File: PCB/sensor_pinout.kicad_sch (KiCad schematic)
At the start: 0 parts

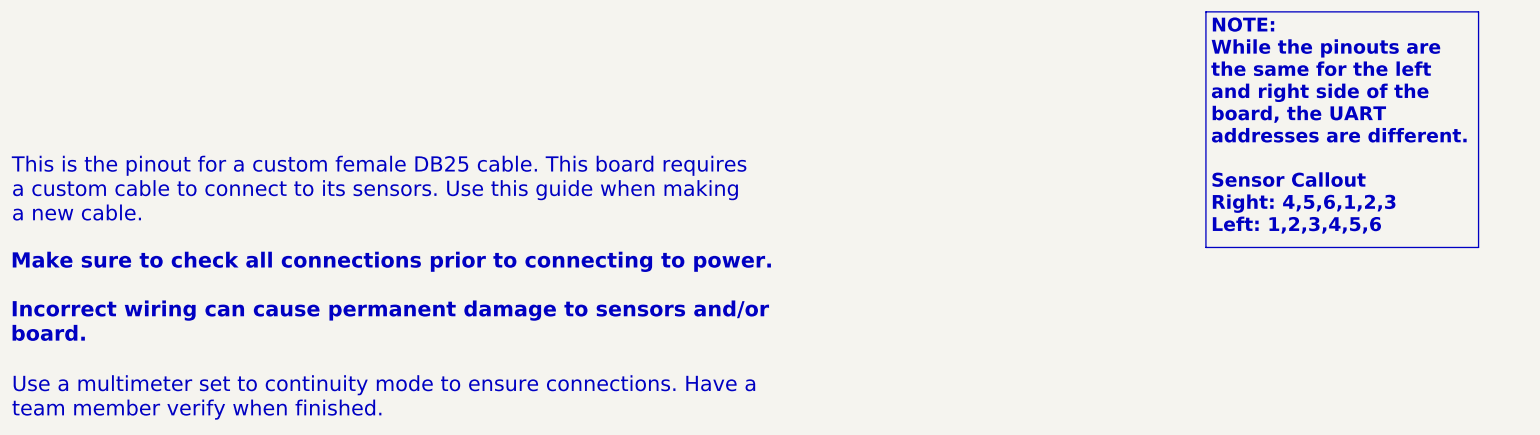
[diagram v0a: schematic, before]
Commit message: Revise PCB footprints, nets and metadata
Refactor multiple footprints and metadata across the DarkMagic PCB files. Removed an obsolete SRN2010 inductor footprint and replaced a capacitor footprint with Inductor_SMD:L_12x12mm_H4.5mm (L1). Standardized net names (e.g. Net-(Q1-G) -> /Q1G), adjusted pad rotations/positions and many silkscreen/fab/crt geometry coordinates, and updated UUIDs and 3D model/part properties. Also updated component reference positions for a few ICs and capacitors and removed a stale KiCad schematic lock file. These edits clean up footprints, ensure consistent metadata and correct layout geometry for fabrication/assembly.
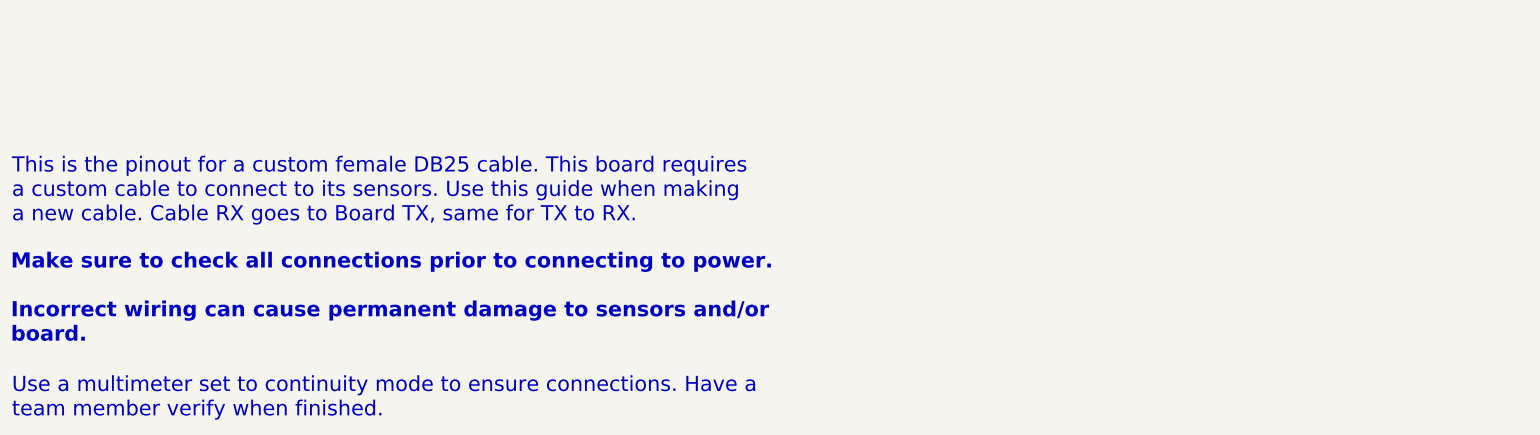
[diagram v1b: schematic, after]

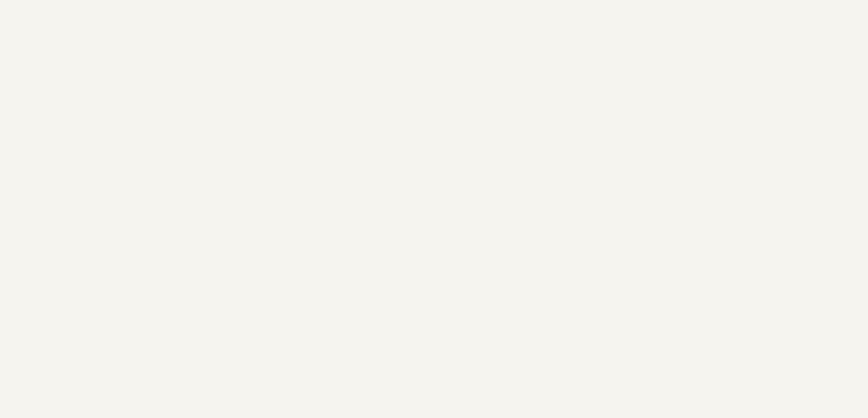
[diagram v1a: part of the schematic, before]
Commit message: Update BOM parts and adjust schematics text/layout
Apply multiple BOM updates and schematic edits: replace/update capacitor, diode, TVS, fuse, regulator, transistor, connector and resistor part numbers and quantities in DarkMagic.csv; add new components (C48/C51/C54, R85-R87, etc.). Change board active layer in DarkMagic.kicad_prl (9 -> 0). Update manufacturer/mouser part numbers for decoupling caps in esp32.kicad_sch and sc16is752_cont..kicad_sch. Tweak sheet text positions/fonts and remove a sentence in sc16is752_cont..kicad_sch, and add a printable installer-sign text block to sensor_pinout.kicad_sch for cable verification. These edits reflect revised part selections and improve schematic documentation/readability.
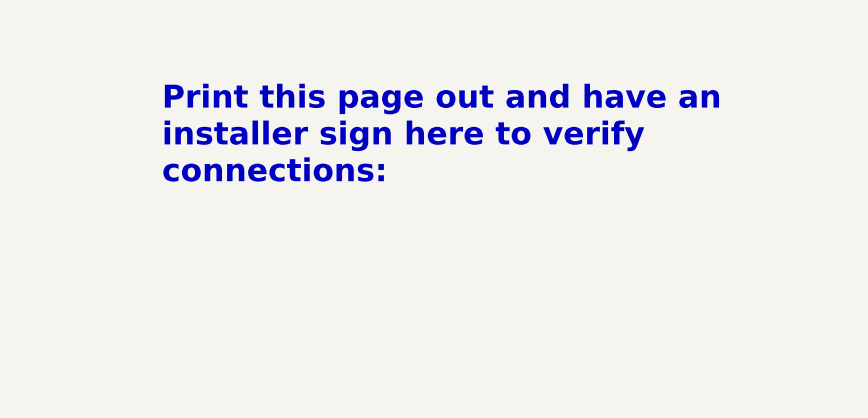
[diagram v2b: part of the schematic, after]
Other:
- note added: "Print this page out and have an installer sign here to verify connections:"
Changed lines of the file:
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@@
+		)
+	)
+	(text "Print this page out and have an\ninstaller sign here to verify\nconnections:"
+		(exclude_from_sim no)
+		(at 177.038 159.512 0)
+		(effects
+			(font
+				(size 2.54 2.54)
+				(thickness 0.508)
+				(bold yes)
+			)
+			(justify left)
 		)
 	)
